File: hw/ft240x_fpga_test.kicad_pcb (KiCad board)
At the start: 4 copper layers, 114 parts, among them J1 Ext_Power, J2 USB_B_Micro, J3 Jtag_Master, J4 JTAG, J5 GPIO_2V5, J6 GPIO_1V8, J7 BNC, J8 BNC, J9 Conn_02x04_Odd_Even, Q1 Si3477, U1 TLV62569DDC, U2 TLV62569DDC, U3 TLV62569DDC, U4 FT240XS, U5 XC3S50A-VQ100, U6 AT25DF041B, U7 5P49V5925, Y1 25MHz

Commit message: several updates...
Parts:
- added C50: 100n, Capacitor_SMD:C_0603_1608Metric, F.Cu at (171.2, 56.1)
- added C51: 100n, Capacitor_SMD:C_0603_1608Metric, F.Cu at (167.6, 51.1)
- added C52: 100n, Capacitor_SMD:C_0603_1608Metric, F.Cu at (163.2, 54.1)
- added C53: 100n, Capacitor_SMD:C_0603_1608Metric, F.Cu at (189.9, 37.1)
- added C54: 30p, Capacitor_SMD:C_0603_1608Metric, F.Cu at (167.2, 54.1)
- added C55: 30p, Capacitor_SMD:C_0603_1608Metric, F.Cu at (163.2, 56.6)
- added C56: 100n, Capacitor_SMD:C_0603_1608Metric, F.Cu at (171.6, 51.1)
- added C57: 100n, Capacitor_SMD:C_0603_1608Metric, F.Cu at (175.6, 51.4)
- added C58: 100n, Capacitor_SMD:C_0603_1608Metric, F.Cu at (171.2, 53.6)
- added C59: 100n, Capacitor_SMD:C_0603_1608Metric, F.Cu at (167.2, 56.6)
- added C60: 100n, Capacitor_SMD:C_0603_1608Metric, F.Cu at (189.9, 39.6)
- added C61: 1u, Capacitor_SMD:C_0805_2012Metric, F.Cu at (163.4, 51.4)
- added C62: 1u, Capacitor_SMD:C_0805_2012Metric, F.Cu at (178.8, 48.7)
- added D10: NSR0170HT1G, Diode_SMD:D_SOD-323, F.Cu at (143.0, 40.6)
- added D11: NSR0170HT1G, Diode_SMD:D_SOD-323, F.Cu at (147.3, 37.7)
- added D12: NSR0170HT1G, Diode_SMD:D_SOD-323, F.Cu at (147.3, 40.6)
- added D9: NSR0170HT1G, Diode_SMD:D_SOD-323, F.Cu at (143.0, 37.7)
- added R30: 1k, Resistor_SMD:R_0603_1608Metric, F.Cu at (183.1, 48.4)
- added R31: 1k, Resistor_SMD:R_0603_1608Metric, F.Cu at (175.2, 53.9)
- added R32: 1k, Resistor_SMD:R_0603_1608Metric, F.Cu at (179.6, 51.4)
- added R33: 1k, Resistor_SMD:R_0603_1608Metric, F.Cu at (189.9, 42.1)
- added R34: 1k, Resistor_SMD:R_0603_1608Metric, F.Cu at (175.2, 56.4)
- added R35: 1k, Resistor_SMD:R_0603_1608Metric, F.Cu at (179.2, 53.9)
- added R36: 1k, Resistor_SMD:R_0603_1608Metric, F.Cu at (187.1, 48.4)
- added R37: 1k, Resistor_SMD:R_0603_1608Metric, F.Cu at (189.9, 44.6)
- added R38: 100, Resistor_SMD:R_0603_1608Metric, F.Cu at (183.6, 50.9)
- added R39: 100, Resistor_SMD:R_0603_1608Metric, F.Cu at (179.2, 56.4)
- added R40: 100, Resistor_SMD:R_0603_1608Metric, F.Cu at (183.2, 53.9)
- added R41: 100, Resistor_SMD:R_0603_1608Metric, F.Cu at (191.1, 47.1)
- added U8: THS4522, Package_SO:TSSOP-16_4.4x5mm_P0.65mm, F.Cu at (143.6, 63.5)
- added U9: MAX19507, Package_QFP:TQFP-48-1EP_7x7mm_P0.5mm_EP5x5mm_ThermalVias, F.Cu at (131.9, 64.7)
- J6: value GPIO_1V8 -> BNC; footprint Connector_PinHeader_2.54mm:PinHeader_2x08_P2.54mm_Vertical -> proj_footprints:BNC_Molex_0731713150
- moved J6 133.2 mm to (170.5, 44.7)
- moved C38 70.9 mm to (110.2, 55.9), turned to 90 degrees
- moved R6 69.1 mm to (64.9, 77.4), turned to 90 degrees
- moved J1 67.7 mm to (66.5, 65.5), turned to 270 degrees
- moved C4 67.6 mm to (67.2, 78.1), turned to 0 degrees
- moved J2 66.8 mm to (66.5, 56.7), turned to 270 degrees
- moved J8 66.2 mm to (159.4, 63.4), turned to 90 degrees
- moved R2 66.1 mm to (67.2, 76.6), turned to 0 degrees
- moved R5 65.6 mm to (64.9, 73.7), turned to 90 degrees
- moved U1 63.1 mm to (67.6, 74.1), turned to 180 degrees
- moved C1 61.5 mm to (66.5, 71.1), turned to 0 degrees
- moved NT1 60.5 mm to (68.7, 72.6), turned to 90 degrees
- moved L1 59.4 mm to (72.3, 75.0), turned to 180 degrees
- moved Q1 56.3 mm to (72.1, 68.2)
- moved C14 56.3 mm to (71.8, 53.8), turned to 0 degrees
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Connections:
- J6 pad 2: +1V8 -> GNDA
- J8 pad 2: GND -> GNDA
- R28 pad 1: Net-(J8-Pad1) -> ADC_CLK
- U5 pad 10: Net-(J6-Pad13) -> FIFO_D5
- U5 pad 12: Net-(J6-Pad11) -> FIFO_D7
- U5 pad 13: Net-(J6-Pad9) -> FIFO_D1
- U5 pad 15: Net-(J6-Pad7) -> FIFO_D2
- U5 pad 16: Net-(J6-Pad5) -> FIFO_D4
- U5 pad 19: Net-(J6-Pad3) -> FIFO_RXE
- U5 pad 20: Net-(J6-Pad1) -> FIFO_D0
- U5 pad 3: Net-(U5-Pad3) -> FIFO_WRb
- U5 pad 4: Net-(U5-Pad4) -> FIFO_RDb
- U5 pad 5: Net-(U5-Pad4) -> FIFO_SIWU
- U5 pad 56: FIFO_WRb -> ADC_D7
- U5 pad 57: FIFO_RDb -> ADC_D6
- U5 pad 59: FIFO_SIWU -> ADC_D5
- U5 pad 6: Net-(U5-Pad6) -> FIFO_D3
- U5 pad 60: FIFO_D3 -> ADC_D4
- U5 pad 61: FIFO_D6 -> ADC_D3
- U5 pad 62: FIFO_D5 -> ADC_D2
- U5 pad 64: FIFO_D7 -> ADC_D1
- U5 pad 65: FIFO_D1 -> ADC_D0
- U5 pad 68: FIFO_D2 -> Net-(U5-Pad68)
- U5 pad 7: Net-(U5-Pad6) -> FIFO_TXF
- U5 pad 70: FIFO_TXF -> ADC_DOR
- U5 pad 71: FIFO_D4 -> Net-(U5-Pad71)
- U5 pad 72: FIFO_RXE -> Net-(U5-Pad71)
- U5 pad 73: FIFO_D0 -> Net-(U5-Pad73)
- U5 pad 83: FIFO_CLK -> ADC_DCLK
- U5 pad 84: Net-(U5-Pad84) -> FPGA_CLK
- U5 pad 85: Net-(U5-Pad85) -> ADC_SDIO
- U5 pad 86: Net-(U5-Pad86) -> ADC_SYNC
- U5 pad 88: Net-(U5-Pad88) -> ADC_SCLK
- U5 pad 89: Net-(U5-Pad89) -> ADC_CSb
- U5 pad 9: Net-(J6-Pad15) -> FIFO_D6
- U5 pad 90: FPGA_CLK -> FIFO_CLK
- U5 pad 93: I2C_SCL -> I2C_SDA
- U5 pad 94: I2C_SDA -> I2C_SCL
- U7 pad 11: Net-(R28-Pad2) -> Net-(R26-Pad2)
- U7 pad 14: Net-(R27-Pad2) -> Net-(U7-Pad14)
- U7 pad 17: Net-(U7-Pad17) -> Net-(R28-Pad2)
- U7 pad 20: Net-(R26-Pad2) -> Net-(R27-Pad2)
- Y1 pad 1: Net-(U7-Pad3) -> Net-(U7-Pad4)
- Y1 pad 3: Net-(U7-Pad4) -> Net-(U7-Pad3)
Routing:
- net GND: track 111.1 -> 162.2 mm, vias 128 -> 191
- net I2C_SDA: track 0.00 -> 43.0 mm, vias 0 -> 3
- net +1V8: track 35.5 -> 75.4 mm, vias 28 -> 71
- net I2C_SCL: track 0.00 -> 34.4 mm, vias 0 -> 2
- net Net-(R5-Pad1): track 56.2 -> 23.9 mm
- net ADC_DCLK: track 0.00 -> 29.4 mm
- net /fpga_xc3s/TCK: track 11.1 -> 38.6 mm, vias 0 -> 1
- net ADC_D0: track 0.00 -> 24.0 mm
- net ADC_D1: track 0.00 -> 22.4 mm
- net ADC_D6: track 0.00 -> 22.0 mm
- net ADC_D5: track 0.00 -> 21.7 mm
- net ADC_D7: track 0.00 -> 21.5 mm
- net ADC_D3: track 0.00 -> 21.0 mm
- net ADC_D4: track 0.00 -> 20.9 mm
- net FPGA_CLK: track 0.00 -> 20.9 mm
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- added copper zone on F.Cu, net Net-(C18-Pad2)
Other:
- rule trace_min: 0.0889 -> 0

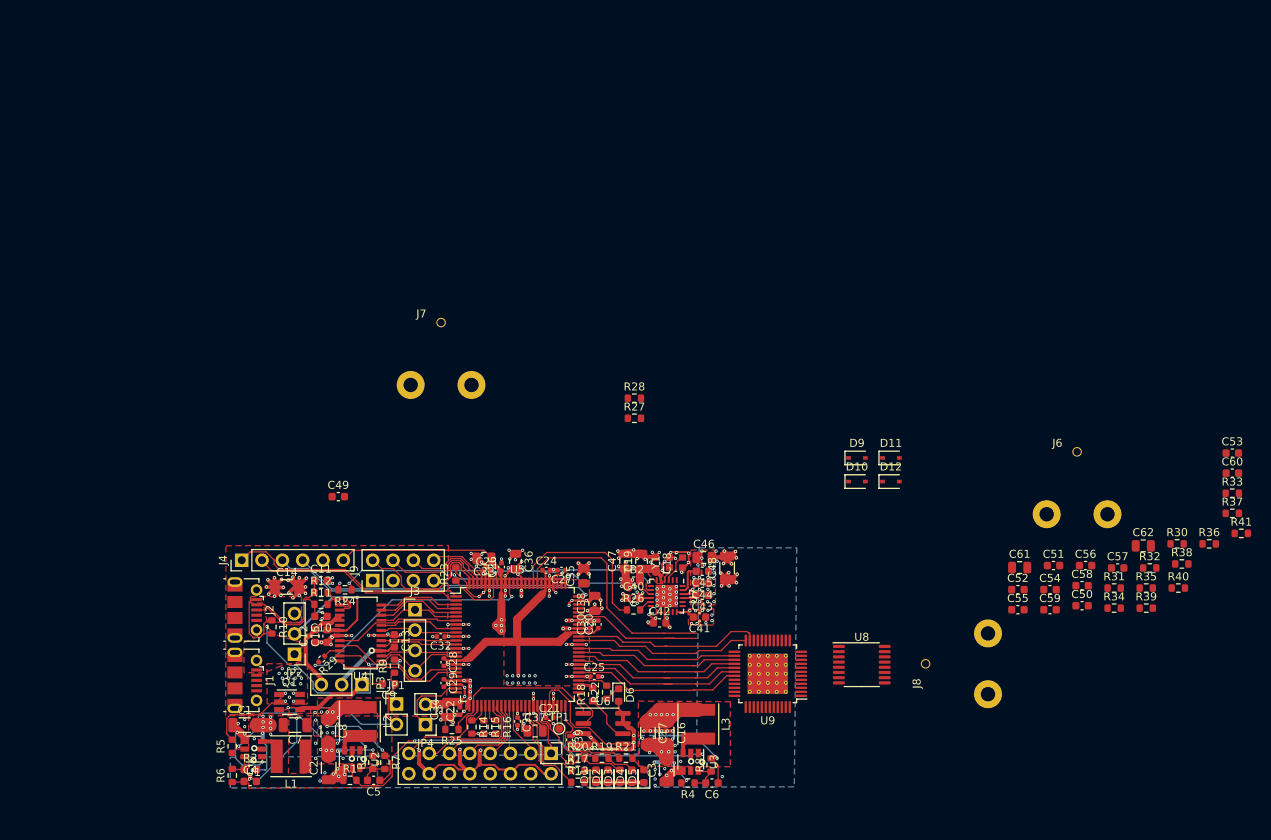
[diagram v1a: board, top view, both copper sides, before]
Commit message: Started to work on analog front-end; ADC connected to fpga
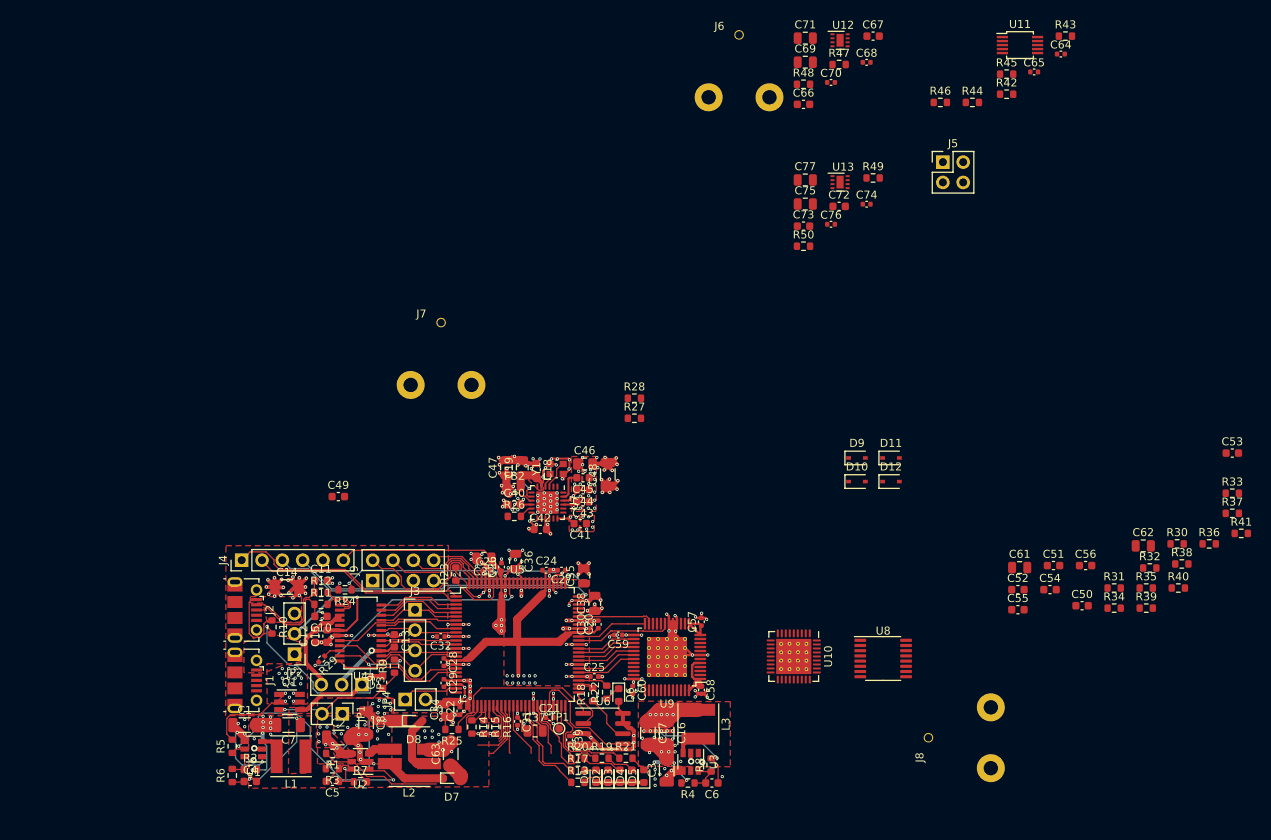
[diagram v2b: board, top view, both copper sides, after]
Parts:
- added C63: 10u, Capacitor_SMD:C_1206_3216Metric, F.Cu at (92.2, 74.7)
- added C64: 100n, Capacitor_SMD:C_0402_1005Metric, F.Cu at (168.5, -12.8)
- added C65: 100n, Capacitor_SMD:C_0402_1005Metric, F.Cu at (165.2, -10.6)
- added C66: 100n, Capacitor_SMD:C_0603_1608Metric, F.Cu at (136.3, -6.53)
- added C67: 100n, Capacitor_SMD:C_0603_1608Metric, F.Cu at (145.1, -15.1)
- added C68: 100n, Capacitor_SMD:C_0402_1005Metric, F.Cu at (144.2, -11.8)
- added C69: 1u, Capacitor_SMD:C_0805_2012Metric, F.Cu at (136.6, -11.8)
- added C70: 100n, Capacitor_SMD:C_0402_1005Metric, F.Cu at (139.8, -9.27)
- added C71: 1u, Capacitor_SMD:C_0805_2012Metric, F.Cu at (136.6, -14.8)
- added C72: 100n, Capacitor_SMD:C_0603_1608Metric, F.Cu at (140.8, 6.22)
- added C73: 100n, Capacitor_SMD:C_0603_1608Metric, F.Cu at (136.3, 8.69)
- added C74: 100n, Capacitor_SMD:C_0402_1005Metric, F.Cu at (144.2, 5.95)
- added C75: 1u, Capacitor_SMD:C_0805_2012Metric, F.Cu at (136.6, 5.93)
- added C76: 100n, Capacitor_SMD:C_0402_1005Metric, F.Cu at (139.8, 8.46)
- added C77: 1u, Capacitor_SMD:C_0805_2012Metric, F.Cu at (136.6, 2.92)
- added D7: CTS05S30, proj_footprints:sod323, F.Cu at (92.4, 77.7)
- added D8: CTS05S30, proj_footprints:sod323-special, F.Cu at (87.6, 70.5)
- added R42: 250, Resistor_SMD:R_0603_1608Metric, F.Cu at (161.7, -7.80)
- added R43: 232, Resistor_SMD:R_0603_1608Metric, F.Cu at (169.1, -15.1)
- added R44: 232, Resistor_SMD:R_0603_1608Metric, F.Cu at (157.5, -6.77)
- added R45: 232, Resistor_SMD:R_0603_1608Metric, F.Cu at (161.7, -10.3)
- added R46: 232, Resistor_SMD:R_0603_1608Metric, F.Cu at (153.4, -6.77)
- added R47: 1k, Resistor_SMD:R_0603_1608Metric, F.Cu at (140.8, -11.5)
- added R48: 1k, Resistor_SMD:R_0603_1608Metric, F.Cu at (136.3, -9.04)
- added R49: 1k, Resistor_SMD:R_0603_1608Metric, F.Cu at (145.1, 2.67)
- added R50: 1k, Resistor_SMD:R_0603_1608Metric, F.Cu at (136.3, 11.2)
- added U10: LMH6882, Package_DFN_QFN:Texas_S-PVQFN-N36_EP4.4x4.4mm_ThermalVias, F.Cu at (135.1, 62.5)
- added U11: MCP47CVB02-E_UN, Package_SO:MSOP-10_3x3mm_P0.5mm, F.Cu at (163.4, -13.9)
- added U12: OPA859xDSG, Package_SON:WSON-8-1EP_2x2mm_P0.5mm_EP0.9x1.6mm, F.Cu at (140.9, -14.5)
- added U13: OPA859xDSG, Package_SON:WSON-8-1EP_2x2mm_P0.5mm_EP0.9x1.6mm, F.Cu at (140.9, 3.19)
- C54, C55: value 30p -> 8p
- C57, C58, C59, C60: footprint Capacitor_SMD:C_0603_1608Metric -> Capacitor_SMD:C_0402_1005Metric
- J5: value GPIO_2V5 -> GPIO2V5; footprint Connector_PinHeader_2.54mm:PinHeader_2x08_P2.54mm_Vertical -> Connector_PinHeader_2.54mm:PinHeader_2x02_P2.54mm_Vertical
- L2: value 2u2 -> 2.2u; footprint Inductor_SMD:L_Taiyo-Yuden_NR-50xx -> proj_footprints:L_Taiyo-Yuden_NR-50xx+bourns0703
- R38, R39, R40, R41: value 100 -> 176
- moved J5 88.7 mm to (153.8, 0.69), turned to 0 degrees
- moved C60 79.7 mm to (115.0, 66.7), turned to 270 degrees
- moved J6 67.1 mm to (128.3, -7.42)
- moved C59 54.1 mm to (113.2, 59.8), turned to 180 degrees
- moved C57 52.5 mm to (123.6, 58.1), turned to 90 degrees
- moved C58 49.3 mm to (123.6, 66.7), turned to 270 degrees
- moved C19 18.9 mm to (101.2, 38.9)
- moved C46 18.9 mm to (109.0, 38.4)
- moved Y1 18.9 mm to (105.5, 39.0)
- moved C40 18.9 mm to (100.2, 43.5)
- moved C41 18.9 mm to (108.4, 45.9)
- moved FB2 18.9 mm to (100.2, 41.4)
- moved U7 18.9 mm to (104.3, 43.2)
- moved C18 18.9 mm to (102.9, 39.1)
- moved C42 18.9 mm to (103.5, 46.6)
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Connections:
- C57 pad 1: GND -> +1V8_analog
- C57 pad 2: +1V8_analog -> GND
- C58 pad 1: GND -> +1V8_analog
- C58 pad 2: +1V8_analog -> GND
- C59 pad 1: GND -> +1V8
- C59 pad 2: +1V8 -> GND
- C60 pad 1: GND -> +1V8
- C60 pad 2: +1V8 -> GND
- J3 pad 2: FIFO_D7 -> FIFO_D5
- J6 pad 1: Net-(J6-Pad1) -> Net-(C66-Pad1)
- J8 pad 1: Net-(J8-Pad1) -> Net-(C72-Pad1)
- L2 pad 1: +2V5 -> Net-(D7-Pad1)
- R1 pad 2: Net-(R1-Pad2) -> PG2V5
- R30 pad 2: GNDA -> Net-(R30-Pad2)
- R31 pad 2: Net-(J6-Pad1) -> /ADC+Driver/buffer/OUT
- R32 pad 2: GNDA -> Net-(R32-Pad2)
- R33 pad 2: Net-(J8-Pad1) -> /ADC+Driver/sheet611E90A8/OUT
- R34 pad 1: Net-(R34-Pad1) -> /ADC+Driver/PGA_INA_P
- R35 pad 1: Net-(R35-Pad1) -> /ADC+Driver/PGA_INA_N
- R36 pad 1: Net-(R36-Pad1) -> /ADC+Driver/PGA_INB_P
- R37 pad 1: Net-(R37-Pad1) -> /ADC+Driver/PGA_INB_N
- R38 pad 2: Net-(R34-Pad1) -> Net-(R38-Pad2)
- R39 pad 2: Net-(R35-Pad1) -> Net-(R39-Pad2)
- R40 pad 2: Net-(R36-Pad1) -> Net-(R40-Pad2)
- R41 pad 2: Net-(R37-Pad1) -> Net-(R41-Pad2)
- U2 pad 5: Net-(R1-Pad2) -> PG2V5
- U3 pad 1: Net-(R1-Pad2) -> PG2V5
- U5 pad 28: Net-(J5-Pad15) -> Net-(J5-Pad3)
- U5 pad 32: Net-(J5-Pad13) -> Net-(J5-Pad1)
- U5 pad 33: Net-(J5-Pad11) -> Net-(U5-Pad33)
- U5 pad 34: Net-(J5-Pad9) -> Net-(U5-Pad34)
- U5 pad 35: Net-(J5-Pad7) -> PGA_SDI
- U5 pad 36: Net-(J5-Pad5) -> PGA_SCLK
- U5 pad 37: Net-(J5-Pad3) -> PGA_CSb
- U5 pad 43: Net-(J5-Pad1) -> PGA_SDO
- U5 pad 64: ADC_D1 -> ADC_DOR
- U5 pad 65: ADC_D0 -> ADC_D1
- U5 pad 70: ADC_DOR -> ADC_D0
- U8 pad 1: PG2V5 -> Net-(U8-Pad1)
- U8 pad 10: Net-(R36-Pad1) -> /ADC+Driver/PGA_INB_P
- U8 pad 11: Net-(R37-Pad1) -> /ADC+Driver/PGA_INB_N
- U8 pad 14: Net-(R34-Pad1) -> /ADC+Driver/PGA_INA_P
- U8 pad 15: Net-(R35-Pad1) -> /ADC+Driver/PGA_INA_N
- U8 pad 5: PG2V5 -> Net-(U8-Pad5)
- U9 pad 11: Net-(C53-Pad2) -> Net-(C65-Pad1)
- U9 pad 2: Net-(C52-Pad2) -> Net-(C64-Pad2)
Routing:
- net Net-(R1-Pad2): track 50.6 -> 0.00 mm, vias 2 -> 0
- net ADC_DCLK: track 29.4 -> 0.00 mm
- net GND: track 162.2 -> 191.4 mm, vias 191 -> 222
- net +2V5: track 121.1 -> 95.7 mm, vias 41 -> 38
- net FPGA_CLK: track 20.9 -> 0.00 mm
- net PG2V5: track 0.00 -> 15.8 mm
- net Net-(J5-Pad13): track 14.5 -> 0.00 mm
- net ADC_D6: track 22.0 -> 7.62 mm
- net ADC_D0: track 24.0 -> 9.63 mm
- net ADC_D5: track 21.7 -> 7.39 mm
- net +1V8_analog: track 0.00 -> 14.1 mm
- net ADC_D7: track 21.5 -> 7.57 mm
- net ADC_D3: track 21.0 -> 7.36 mm
- net ADC_D4: track 20.9 -> 7.39 mm
- net ADC_D1: track 22.4 -> 8.95 mm
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- added copper zone on F.Cu, net +5V
- removed copper zone on B.Cu, net +5V

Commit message: more work (don't recall details :-()
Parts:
- removed the C49 at (78.2, 42.5)
- added C100: 100n, Capacitor_SMD:C_0603_1608Metric, F.Cu at (69.8, 41.8)
- added C57: 10n, Capacitor_SMD:C_0402_1005Metric, F.Cu at (136.4, 68.1)
- added C78: 100n, Capacitor_SMD:C_0402_1005Metric, F.Cu at (128.8, 41.0)
- added C79: 1u, Capacitor_SMD:C_0805_2012Metric, F.Cu at (128.7, 43.2)
- added C80: 100n, Capacitor_SMD:C_0402_1005Metric, F.Cu at (134.2, 45.5)
- added C81: 1u, Capacitor_SMD:C_0805_2012Metric, F.Cu at (134.2, 43.3)
- added C82: 100n, Capacitor_SMD:C_0603_1608Metric, F.Cu at (116.2, 42.0)
- added C83: 10n, Capacitor_SMD:C_0402_1005Metric, F.Cu at (136.4, 58.9)
- added C84: 10n, Capacitor_SMD:C_0402_1005Metric, F.Cu at (137.4, 58.9)
- added C85: 2n, Capacitor_SMD:C_0603_1608Metric, F.Cu at (133.5, 38.9)
- added C86: 2n, Capacitor_SMD:C_0603_1608Metric, F.Cu at (133.5, 48.3)
- added C87: 100n, Capacitor_SMD:C_0603_1608Metric, F.Cu at (153.8, 64.3)
- added C88: 100n, Capacitor_SMD:C_0603_1608Metric, F.Cu at (153.8, 62.8)
- added C89: 1u, Capacitor_SMD:C_0805_2012Metric, F.Cu at (137.4, 39.4)
- added C90: 1u, Capacitor_SMD:C_0805_2012Metric, F.Cu at (137.4, 47.8)
- added C91: 10n, Capacitor_SMD:C_0402_1005Metric, F.Cu at (137.4, 68.1)
- added C92: 15p, Capacitor_SMD:C_0603_1608Metric, F.Cu at (130.3, 67.1)
- added C93: 15p, Capacitor_SMD:C_0603_1608Metric, F.Cu at (130.3, 57.9)
- added C94: 10n, Capacitor_SMD:C_0402_1005Metric, F.Cu at (142.9, 68.3)
- added C95: 10n, Capacitor_SMD:C_0402_1005Metric, F.Cu at (143.0, 58.7)
- added C96: 1u, Capacitor_SMD:C_0805_2012Metric, F.Cu at (141.0, 70.0)
- added C97: 1u, Capacitor_SMD:C_0805_2012Metric, F.Cu at (140.0, 58.2)
- added C98: 5-15p, proj_footprints:C_Trimmer_EW_Electronics_SCG3S, F.Cu at (148.4, 77.1)
- added C99: 5-15p, proj_footprints:C_Trimmer_EW_Electronics_SCG3S, F.Cu at (148.2, 50.7)
- added J11: PEN_SEL, Connector_PinHeader_2.54mm:PinHeader_2x03_P2.54mm_Vertical, F.Cu at (77.1, 45.0)
- added R51: 5k, Resistor_SMD:R_0603_1608Metric, F.Cu at (129.7, 38.2)
- added R52: 10k, Resistor_SMD:R_0603_1608Metric, F.Cu at (132.0, 38.9)
- added R53: 5k, Resistor_SMD:R_0603_1608Metric, F.Cu at (129.8, 49.0)
- added R54: 10k, Resistor_SMD:R_0603_1608Metric, F.Cu at (132.0, 48.3)
- added R55: 10k, Resistor_SMD:R_0603_1608Metric, F.Cu at (129.7, 39.7)
- added R56: 10k, Resistor_SMD:R_0603_1608Metric, F.Cu at (129.8, 47.6)
- added R57: 232, Resistor_SMD:R_0603_1608Metric, F.Cu at (125.2, 64.3)
- added R58: 5k, Resistor_SMD:R_0603_1608Metric, F.Cu at (134.9, 38.9)
- added R59: 232, Resistor_SMD:R_0603_1608Metric, F.Cu at (125.2, 60.7)
- added R60: 5k, Resistor_SMD:R_0603_1608Metric, F.Cu at (134.9, 48.3)
- added R61: 1, Resistor_SMD:R_0603_1608Metric, F.Cu at (136.1, 41.9)
- added R62: 1, Resistor_SMD:R_0603_1608Metric, F.Cu at (136.1, 45.3)
- added R63: 10k, Resistor_SMD:R_0603_1608Metric, F.Cu at (71.7, 52.0)
- added R64: 10k, Resistor_SMD:R_0603_1608Metric, F.Cu at (76.2, 51.1)
- added R65: 5k1, Resistor_SMD:R_0603_1608Metric, F.Cu at (73.2, 52.0)
- added R66: 5k1, Resistor_SMD:R_0603_1608Metric, F.Cu at (79.2, 51.4)
- added R67: 10k, Resistor_SMD:R_0603_1608Metric, F.Cu at (66.0, 40.1)
- added R68: 10k, Resistor_SMD:R_0603_1608Metric, F.Cu at (67.5, 40.1)
- added R69: 5k1, Resistor_SMD:R_0603_1608Metric, F.Cu at (69.8, 40.3)
- added R70: 35k7, Resistor_SMD:R_0603_1608Metric, F.Cu at (66.8, 37.9)
- added R71: 100k, Resistor_SMD:R_0603_1608Metric, F.Cu at (71.2, 38.8)
- added R72: 100k, Resistor_SMD:R_0603_1608Metric, F.Cu at (79.7, 42.0)
- added U14: MCP47CVB02-E_UN, Package_SO:MSOP-10_3x3mm_P0.5mm, F.Cu at (116.9, 39.3)
- added U15: UTC2000, Package_DFN_QFN:QFN-16-1EP_3x3mm_P0.5mm_EP1.75x1.75mm_ThermalVias, F.Cu at (70.7, 44.6)
- added U16: 74LVC1G32, Package_TO_SOT_SMD:SOT-353_SC-70-5, F.Cu at (80.3, 45.1)
- C54, C55: value 8p -> 15p
- C56, R34, R35, R36, R37: moved to B.Cu
- C66, C72: value 100n -> 20p
- C67, C73: value 100n -> 10p
- J2: value USB_B_Micro -> USB_C_Receptacle_USB2.0; footprint Connector_USB:USB_Micro-B_Molex-105017-0001 -> proj_footprints:USB_C_Receptacle_GCT_USB4085_smaller_holes
- J5: footprint Connector_PinHeader_2.54mm:PinHeader_2x02_P2.54mm_Vertical -> Connector_PinHeader_2.54mm:PinHeader_2x03_P2.54mm_Vertical
- R10: value 100k -> 47k
- R47, R48, R49, R50: value 1k -> 500k
- U11: value MCP47CVB02-E_UN -> TSV992A; footprint Package_SO:MSOP-10_3x3mm_P0.5mm -> Package_SO:MSOP-8_3x3mm_P0.65mm
- moved R42 102.7 mm to (104.0, 77.2)
- moved J5 96.1 mm to (95.7, 77.2), turned to 90 degrees
- moved R43 91.5 mm to (128.8, 67.1), turned to 270 degrees
- moved C67 89.5 mm to (146.2, 74.5)
- moved C64 87.3 mm to (134.5, 67.6)
- moved J6 86.5 mm to (159.1, 73.4), turned to 90 degrees
- moved C71 85.9 mm to (144.9, 70.6), turned to 180 degrees
- moved U12 85.5 mm to (148.9, 70.6), turned to 90 degrees
- moved R47 84.9 mm to (149.1, 72.9)
- moved R48 82.6 mm to (146.2, 72.9)
- moved C66 82.0 mm to (149.1, 74.5), turned to 180 degrees
- moved C68 81.9 mm to (150.6, 69.8), turned to 270 degrees
- moved C69 80.3 mm to (152.8, 66.8)
- moved C70 79.5 mm to (147.1, 69.8), turned to 270 degrees
- moved R45 78.5 mm to (128.8, 61.0), turned to 270 degrees
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- renumbered C57 to C49
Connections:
- net PG2V5 renamed Net-(R1-Pad2)
- C49 pad 2: GND -> GNDA
- C54 pad 1: /ADC+Driver/INA_P -> /ADC+Driver/INA_N
- C54 pad 2: /ADC+Driver/INA_N -> GND
- C55 pad 1: /ADC+Driver/INB_P -> GND
- C55 pad 2: /ADC+Driver/INB_N -> /ADC+Driver/INB_P
- C58 pad 2: GND -> GNDA
- C64 pad 1: GND -> GNDA
- C65 pad 2: GND -> GNDA
- C68 pad 2: GND -> GNDA
- C69 pad 2: GND -> GNDA
- C70 pad 2: GND -> GNDA
- C71 pad 2: GND -> GNDA
- C74 pad 2: GND -> GNDA
- C75 pad 2: GND -> GNDA
- C76 pad 2: GND -> GNDA
- C77 pad 2: GND -> GNDA
- J5 pad 1: Net-(J5-Pad1) -> GND
- J5 pad 4: GND -> Net-(J5-Pad4)
- J7 pad 1: Net-(C49-Pad2) -> Net-(J7-Pad1)
- JP1 pad 2: Net-(C9-Pad1) -> Net-(JP1-Pad2)
- R27 pad 1: Net-(C49-Pad1) -> Net-(J7-Pad1)
- R30 pad 2: Net-(R30-Pad2) -> /ADC+Driver/offset_dac/DAC_0
- R32 pad 2: Net-(R32-Pad2) -> /ADC+Driver/sheet611E90A8/OUT
- R33 pad 2: /ADC+Driver/sheet611E90A8/OUT -> /ADC+Driver/offset_dac/DAC_1
- R9 pad 1: Net-(C9-Pad1) -> Net-(JP1-Pad2)
- U10 pad 1: GND -> GNDA
- U10 pad 16: /ADC+Driver/PGA_INB_P -> /ADC+Driver/PGA_INB_N
- U10 pad 17: /ADC+Driver/PGA_INB_N -> /ADC+Driver/PGA_INB_P
- U10 pad 21: GND -> GNDA
- U10 pad 22: GND -> GNDA
- U10 pad 23: GND -> GNDA
- U10 pad 37: GND -> GNDA
- U10 pad 5: GND -> GNDA
- U10 pad 6: GND -> GNDA
- U11 pad 4: Net-(R32-Pad2) -> -2V5
- U11 pad 5: Net-(R30-Pad2) -> Net-(R53-Pad2)
- U11 pad 6: GNDA -> Net-(C86-Pad2)
- U11 pad 7: GNDA -> Net-(C86-Pad1)
- U11 pad 8: Net-(U11-Pad8) -> +2V5_analog
- U5 pad 32: Net-(J5-Pad1) -> Net-(J5-Pad4)
- U5 pad 33: Net-(U5-Pad33) -> Net-(J5-Pad5)
- U5 pad 34: Net-(U5-Pad34) -> Net-(J5-Pad6)
- U5 pad 35: PGA_SDI -> PGA_SDO
- U5 pad 36: PGA_SCLK -> PGA_SDI
- U5 pad 37: PGA_CSb -> PGA_SCLK
- U5 pad 43: PGA_SDO -> PGA_CSb
- U5 pad 85: ADC_SDIO -> ADC_SYNC
- U5 pad 86: ADC_SYNC -> ADC_CSb
- U5 pad 89: ADC_CSb -> ADC_SDIO
- U9 pad 5: +1V8_analog -> GND
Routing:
- net GNDA: track 0.00 -> 161.6 mm, vias 0 -> 40
- net PGA_SDO: track 6.97 -> 62.5 mm, vias 0 -> 2
- net Net-(JP1-Pad2): track 0.00 -> 52.4 mm, vias 0 -> 1
- net GND: track 191.4 -> 236.2 mm, vias 222 -> 225
- net PGA_SDI: track 7.23 -> 50.0 mm, vias 0 -> 2
- net VBUS: track 9.67 -> 52.4 mm
- net PGA_SCLK: track 6.00 -> 43.8 mm, vias 0 -> 2
- net /ADC+Driver/offset_dac/DAC_0: track 0.00 -> 37.6 mm, vias 0 -> 2
- net Net-(C9-Pad1): track 17.1 -> 53.2 mm, vias 1 -> 3
- net Net-(R1-Pad2): track 15.8 -> 51.4 mm, vias 0 -> 2
- net Net-(R52-Pad1): track 0.00 -> 34.6 mm
- net PGA_CSb: track 6.87 -> 41.1 mm, vias 0 -> 2
- net Vpp_analog: track 0.00 -> 33.4 mm, vias 0 -> 19
- net /ADC+Driver/offset_dac/DAC_1: track 0.00 -> 32.1 mm, vias 0 -> 2
- net Net-(J7-Pad1): track 0.00 -> 31.9 mm
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- added copper zone on In2.Cu, net VBUS
- added copper zone on In2.Cu, net Vpp_analog
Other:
- board outline added: 100 x 42.4 mm
